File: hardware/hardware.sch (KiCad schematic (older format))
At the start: 35 parts

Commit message: fix signal names for I2S, and wrong wiring
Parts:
- added R?: 10k, symbol Device:R
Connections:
- net labels added: I2S_BCK, I2S_DATA, I2S_LRCK, I2S_SCK
- net labels removed: BCK, DIN, LCK, SCK
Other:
- moved on the sheet: R?
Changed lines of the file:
@@
 TRK_PREV
 Text Label 5850 6400 0    50   ~ 0
-LCK
+I2S_LRCK
 Text Label 5850 6300 0    50   ~ 0
-DIN
+I2S_DATA
 Text Label 5850 6500 0    50   ~ 0
-BCK
+I2S_BCK
 Text Label 2150 1900 2    50   ~ 0
 POWER_CTRL
 Text Label 5850 6000 0    50   ~ 0
 POWER_CTRL
-Wire Wire Line
-	8150 5100 8300 5100
-Wire Wire Line
-	8150 5200 8300 5200
-Wire Wire Line
-	8150 5300 8300 5300
 $Comp
 L power:GNDA #PWR?
@@
 	1    0    0    -1
 $EndComp
-Wire Wire Line
-	7500 4850 7500 5000
-Connection ~ 8050 5000
-Wire Wire Line
-	8000 5000 8050 5000
-Wire Wire Line
-	7500 5000 7500 5500
-Connection ~ 7500 5000
-Wire Wire Line
-	7500 5000 7700 5000
 $Comp
 L Device:R R?
 U 1 1 5E73006F
-P 7850 5000
-F 0 "R?" V 7643 5000 50  0000 C CNN
-F 1 "10k" V 7734 5000 50  0000 C CNN
-F 2 "" V 7780 5000 50  0001 C CNN
-F 3 "~" H 7850 5000 50  0001 C CNN
-	1    7850 5000
+P 7700 4700
+F 0 "R?" V 7493 4700 50  0000 C CNN
+F 1 "10k" V 7584 4700 50  0000 C CNN
+F 2 "" V 7630 4700 50  0001 C CNN
+F 3 "~" H 7700 4700 50  0001 C CNN
+	1    7700 4700
 	0    1    1    0
 $EndComp
 Wire Wire Line
 	7500 5500 8000 5500
-Text Label 8150 5100 0    50   ~ 0
-BCK
-Text Label 8150 5200 0    50   ~ 0
-DIN
-Text Label 8150 5300 0    50   ~ 0
-LCK
+Text Label 7950 5100 0    50   ~ 0
+I2S_BCK
+Text Label 7950 5200 0    50   ~ 0
+I2S_DATA
+Text Label 7950 5300 0    50   ~ 0
+I2S_LRCK
 Wire Wire Line
 	7600 5400 8300 5400
@@
 L power:+3.3VDAC #PWR?
 U 1 1 5E7200C0
-P 7500 4850
-F 0 "#PWR?" H 7650 4800 50  0001 C CNN
-F 1 "+3.3VDAC" H 7520 4993 50  0000 C CNN
-F 2 "" H 7500 4850 50  0001 C CNN
-F 3 "" H 7500 4850 50  0001 C CNN
-	1    7500 4850
+P 7500 4500
+F 0 "#PWR?" H 7650 4450 50  0001 C CNN
+F 1 "+3.3VDAC" H 7520 4643 50  0000 C CNN
+F 2 "" H 7500 4500 50  0001 C CNN
+F 3 "" H 7500 4500 50  0001 C CNN
+	1    7500 4500
 	1    0    0    -1
 $EndComp
 Text Label 9050 4700 0    50   ~ 0
 FMT
-Text Label 8150 5000 0    50   ~ 0
-SCK
-Wire Wire Line
-	8050 5000 8300 5000
-Wire Wire Line
-	8050 4700 9150 4700
-Wire Wire Line
-	8050 4700 8050 5000
+Text Label 7950 5000 0    50   ~ 0
+I2S_SCK
 Wire Wire Line
 	9150 4800 9150 4700
@@
 Text Label 5850 5100 0    50   ~ 0
 SD-CS
+Wire Wire Line
+	7950 5200 8300 5200
+Wire Wire Line
+	7950 5300 8300 5300
+Wire Wire Line
+	7950 5100 8300 5100
+Wire Wire Line
+	7500 4500 7500 4700
+Connection ~ 7500 4700
+Wire Wire Line
+	7500 4700 7500 5000
+Wire Wire Line
+	7550 4700 7500 4700
+Wire Wire Line
+	7850 4700 9150 4700
+$Comp
+L Device:R R?
+U 1 1 5EAA3BBD
+P 7700 5000
+F 0 "R?" V 7493 5000 50  0000 C CNN
+F 1 "10k" V 7584 5000 50  0000 C CNN
+F 2 "" V 7630 5000 50  0001 C CNN
+F 3 "~" H 7700 5000 50  0001 C CNN
+	1    7700 5000
+	0    1    1    0
+$EndComp
+Wire Wire Line
+	7550 5000 7500 5000
+Connection ~ 7500 5000
+Wire Wire Line
+	7500 5000 7500 5500
+Wire Wire Line
+	7850 5000 8300 5000
 $EndSCHEMATC

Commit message: some fixes and add ADC measurement for battery voltage
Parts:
- removed C?: C, symbol Device:C
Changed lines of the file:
@@
 Connection ~ 9800 1000
-$Comp
-L Device:C C?
-U 1 1 5E98019E
-P 7350 1150
-F 0 "C?" H 7465 1196 50  0000 L CNN
-F 1 "C" H 7465 1105 50  0000 L CNN
-F 2 "" H 7388 1000 50  0001 C CNN
-F 3 "~" H 7350 1150 50  0001 C CNN
-	1    7350 1150
-	1    0    0    -1
-$EndComp
 $Comp
 L Device:L_Coupled L?
@@
 Wire Wire Line
 	7600 1000 7350 1000
-Connection ~ 7350 1000
 Wire Wire Line
 	7600 1250 7600 1300
 Wire Wire Line
 	7600 1300 7350 1300
-Connection ~ 7350 1300
 Wire Wire Line
 	8000 1050 8000 1000

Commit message: update schematics
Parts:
- removed C?: C, symbol Device:C
- removed D?: D, symbol Device:D
- removed J?: SDCARD, symbol Connector_Generic:Conn_01x06
- removed J?: PAM8403_IN, symbol Connector_Generic:Conn_01x07
- removed J?: PAM8403_OUT, symbol Connector_Generic:Conn_01x07
- removed J?: Power, symbol Connector:Conn_01x03_Male
- removed K?: HE721C0500, DIP952W51P254L1905H550Q14N, symbol HE721C0500:HE721C0500
- removed Q?: BC107, Package_TO_SOT_THT:TO-18-3, symbol Transistor_BJT:BC107
- removed R?: 220, symbol Device:R
- removed U?: TLV1117-33, symbol Regulator_Linear:TLV1117-33
- added C?: 220nF, symbol Device:C
- added C?: 100nF, symbol Device:C
- added C?: 10uF, symbol Device:C
- added C? (x3): 1uF, symbol Device:C
- added C?: 0.1uF, symbol Device:C
- added C? (x4): 0.22uF, symbol Device:C
- added C?: 470uF, symbol Device:CP
- added J?: Screw_Terminal_01x02, symbol Connector:Screw_Terminal_01x02
- added J?: 104031-0811, MOLEX_104031-0811, symbol MicroSD_Slot:104031-0811
- added R? (x3): 100k, symbol Device:R
- added R?: 330k, symbol Device:R
- added R?: 1k, symbol Device:R
- added R? (x6): 47k, symbol Device:R
- added R? (x2): 220k, symbol Device:R
- added U?: PAM8403, symbol pam8403:PAM8403
- added U?: XRP6272, symbol XRP6272:XRP6272
- C? (x2): value C -> 4.7uF
- C?: value CP -> 1.5F
- C? (x2): value C -> 10uF
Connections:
- net labels added: +BATT, VBATT_MEAS
- net labels removed: +5VD, G
- wire segments 124 -> 156
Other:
- moved on the sheet: C?, J?, L?, R?, U?

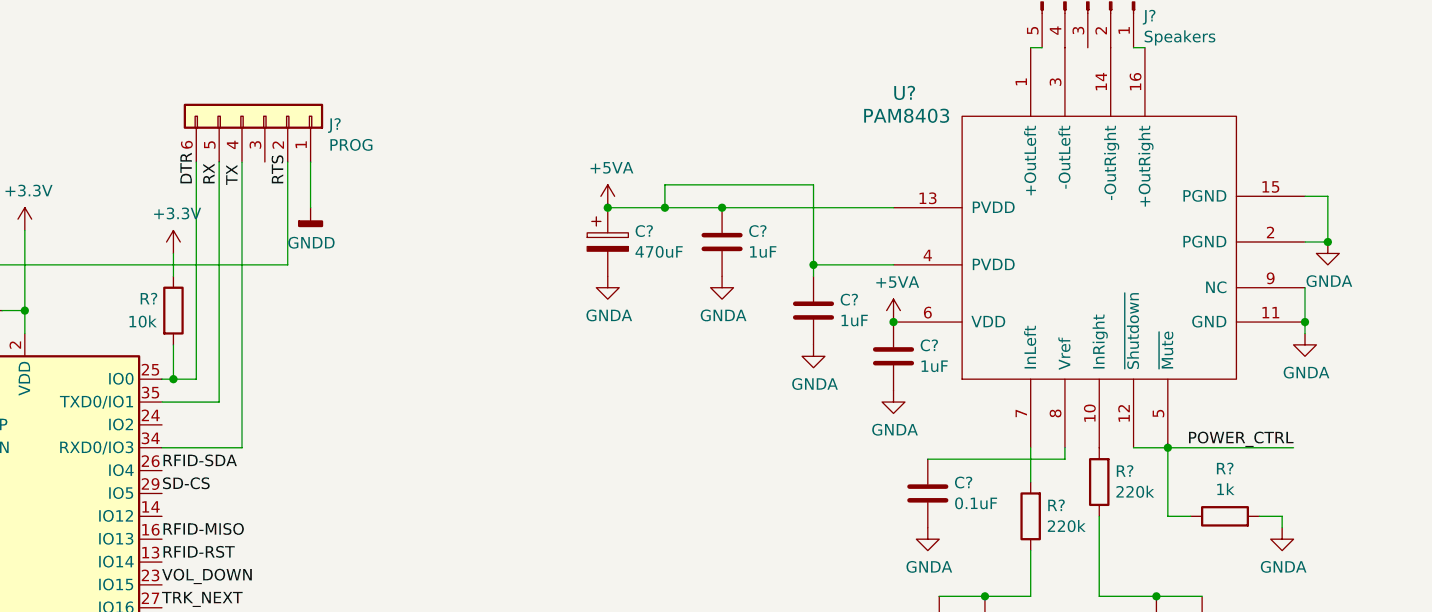
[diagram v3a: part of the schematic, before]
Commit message: correction: amplifier has separate pin for enable
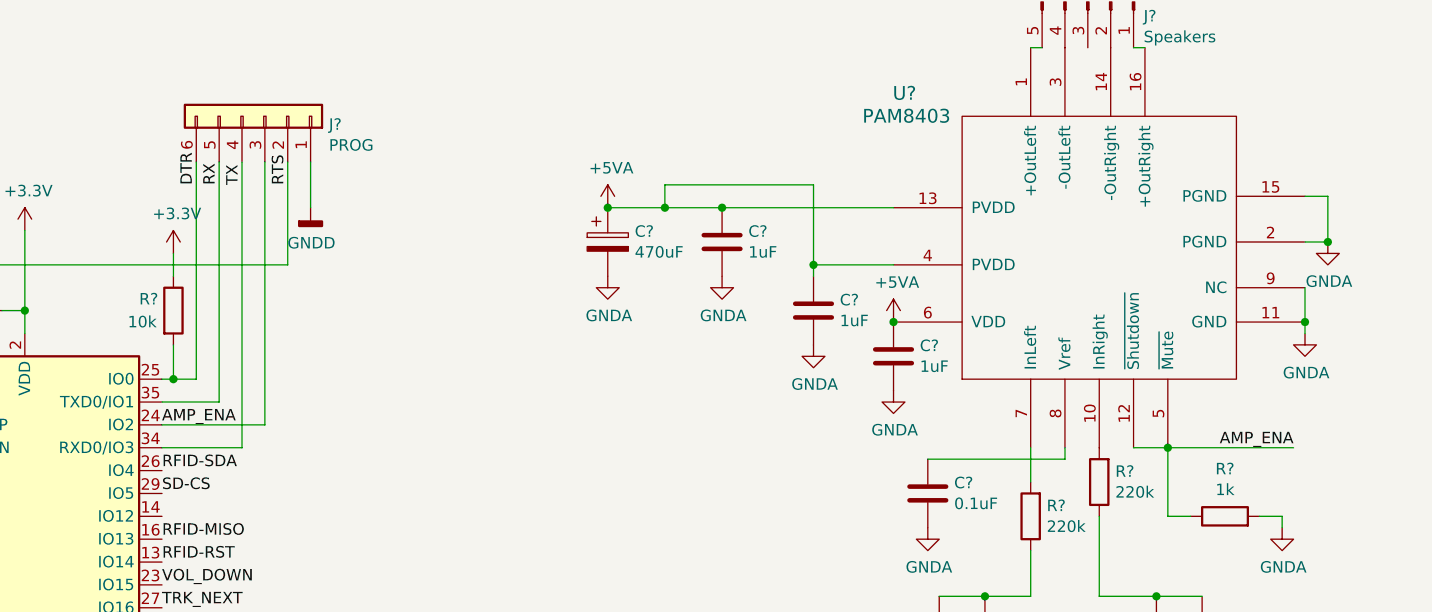
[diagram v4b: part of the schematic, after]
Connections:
- net POWER_CTRL: no longer R?.1, U?.12 (~Shutdown), U?.5 (~Mute)
- net AMP_ENA: now reaches U?.24 (IO2)
- net AMP_ENA: now also J?.3 (Pin_3), R?.1, U?.12 (~Shutdown), U?.5 (~Mute)
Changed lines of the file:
@@
 	8950 1100 9050 1100
 Text Label 10450 3850 2    50   ~ 0
-POWER_CTRL
+AMP_ENA
 Wire Wire Line
 	9750 3850 9900 3850
@@
 Wire Wire Line
 	9950 4800 10050 4800
+Text Label 5500 3750 0    50   ~ 0
+AMP_ENA
+Wire Wire Line
+	5500 3750 5950 3750
+Wire Wire Line
+	5950 3750 5950 2600
 $EndSCHEMATC

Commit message: minor correction
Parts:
- J?: value Screw_Terminal_01x02 -> BATT

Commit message: Reduce coupling capacitor between DAC and amplifier
This is necessary to reduce the pop noise when switching on. The corner frequency is still much lower than the bandwidth of the speakers.
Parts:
- removed C? (x2): 0.22uF, symbol Device:C
- C? (x2): value 0.22uF -> 33nF
- U?: symbol RF_Module:ESP32-WROOM-32 -> hardware-rescue:ESP32-WROOM-32-RF_Module
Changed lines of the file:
@@
 EESchema Schematic File Version 4
+LIBS:hardware-cache
 EELAYER 30 0
 EELAYER END
@@
 $EndDescr
 $Comp
-L RF_Module:ESP32-WROOM-32 U?
+L hardware-rescue:ESP32-WROOM-32-RF_Module U?
 U 1 1 5E6E43BB
 P 4900 4750
@@
 $EndComp
 Wire Wire Line
-	9950 4800 10050 4800
-Connection ~ 9950 4800
-Wire Wire Line
-	9950 4900 9950 4800
-Wire Wire Line
-	9000 4800 9100 4800
-Connection ~ 9000 4800
-Wire Wire Line
-	9000 4900 9000 4800
-Wire Wire Line
 	9850 4500 9600 4500
-Connection ~ 9850 4500
 Wire Wire Line
 	9600 4500 9600 4150
 Wire Wire Line
-	10050 4500 9850 4500
-Connection ~ 9100 4500
-Wire Wire Line
 	9300 4500 9300 4300
 Wire Wire Line
 	9100 4500 9300 4500
-Wire Wire Line
-	9850 4800 9950 4800
-$Comp
-L Device:C C?
-U 1 1 5EFB32FF
-P 10050 4650
-F 0 "C?" H 10165 4696 50  0000 L CNN
-F 1 "0.22uF" H 10165 4605 50  0000 L CNN
-F 2 "" H 10088 4500 50  0001 C CNN
-F 3 "~" H 10050 4650 50  0001 C CNN
-	1    10050 4650
-	1    0    0    -1
-$EndComp
 $Comp
 L Device:C C?
@@
 P 9850 4650
 F 0 "C?" H 10050 4600 50  0000 R CNN
-F 1 "0.22uF" H 10200 4700 50  0000 R CNN
+F 1 "33nF" H 10200 4700 50  0000 R CNN
 F 2 "" H 9888 4500 50  0001 C CNN
 F 3 "~" H 9850 4650 50  0001 C CNN
 	1    9850 4650
-	-1   0    0    1
-$EndComp
-Wire Wire Line
-	8900 4500 9100 4500
-Wire Wire Line
-	8900 4800 9000 4800
-$Comp
-L Device:C C?
-U 1 1 5EF8F703
-P 8900 4650
-F 0 "C?" H 9100 4600 50  0000 R CNN
-F 1 "0.22uF" H 9250 4700 50  0000 R CNN
-F 2 "" H 8938 4500 50  0001 C CNN
-F 3 "~" H 8900 4650 50  0001 C CNN
-	1    8900 4650
 	-1   0    0    1
 $EndComp
@@
 Wire Wire Line
 	9300 3850 9300 4000
-Text Label 9950 4900 0    50   ~ 0
+Text Label 9850 4900 0    50   ~ 0
 R
-Text Label 9000 4900 0    50   ~ 0
+Text Label 9100 4900 0    50   ~ 0
 L
 $Comp
@@
 P 9100 4650
 F 0 "C?" H 9215 4696 50  0000 L CNN
-F 1 "0.22uF" H 9215 4605 50  0000 L CNN
+F 1 "33nF" H 9215 4605 50  0000 L CNN
 F 2 "" H 9138 4500 50  0001 C CNN
 F 3 "~" H 9100 4650 50  0001 C CNN
@@
 	1    0    0    -1
 $EndComp
+Wire Wire Line
+	9850 4900 9850 4800
+Wire Wire Line
+	9100 4900 9100 4800
 $EndSCHEMATC

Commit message: fix ERC errors, separate AMP_UNMUTE from AMP_ENA
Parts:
- added J?: Conn_01x05_Male, symbol Connector:Conn_01x05_Male
- added R19: 1k, symbol Device:R
- U1: renamed from U?; symbol hardware-rescue:ESP32-WROOM-32-RF_Module -> hardware-rescue:ESP32-WROOM-32-RF_Module-hardware-rescue
- gave numbers to parts that had none: 51
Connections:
- net +3V3: now also J?.5 (Pin_5)
- net AMP_ENA: now also R19.1; no longer R20.1, U4.5 (~Mute)
- net GNDA: now also R19.2
- net GNDD: now also J3.G1 (GND), J3.G2 (GND), J3.G3 (GND), J3.G4 (GND), J?.4 (Pin_4)
- net AMP_UNMUTE: now reaches U1.14 (IO12)
- net AMP_UNMUTE: now also R20.1, U4.5 (~Mute)
- net EXT3: now reaches U1.5 (SENSOR_VN)
- net EXT3: now also J?.3 (Pin_3)
- net EXT1: now reaches U1.6 (IO34)
- net EXT1: now also J?.1 (Pin_1)
- net EXT2: now reaches U1.7 (IO35)
- net EXT2: now also J?.2 (Pin_2)
- no-connect marks 0 -> 15
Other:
- moved on the sheet: R20

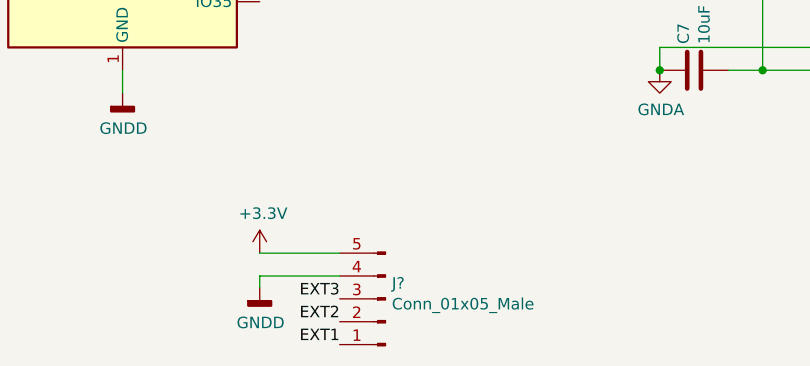
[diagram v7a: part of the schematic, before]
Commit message: fix missing annotation
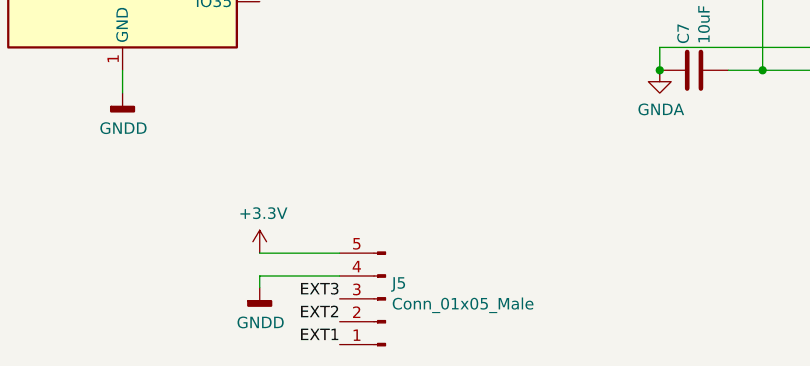
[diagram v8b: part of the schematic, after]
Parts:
- gave numbers to parts that had none: 1
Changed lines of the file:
@@
 	9750 3850 10500 3850
 $Comp
-L Connector:Conn_01x05_Male J?
+L Connector:Conn_01x05_Male J5
 U 1 1 5ED9429D
 P 6050 7150
-F 0 "J?" H 6022 7082 50  0000 R CNN
+F 0 "J5" H 6022 7082 50  0000 R CNN
 F 1 "Conn_01x05_Male" H 6022 7173 50  0000 R CNN
 F 2 "" H 6050 7150 50  0001 C CNN
